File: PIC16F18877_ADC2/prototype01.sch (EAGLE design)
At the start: 18 parts, among them CN1 PIC_CN_H, CN2 12V_IN, CN3 ADC_IN, SW1 10-XX, U1 XC6202P502TB, U2 PIC16F18877-I/P, X1 20MHz

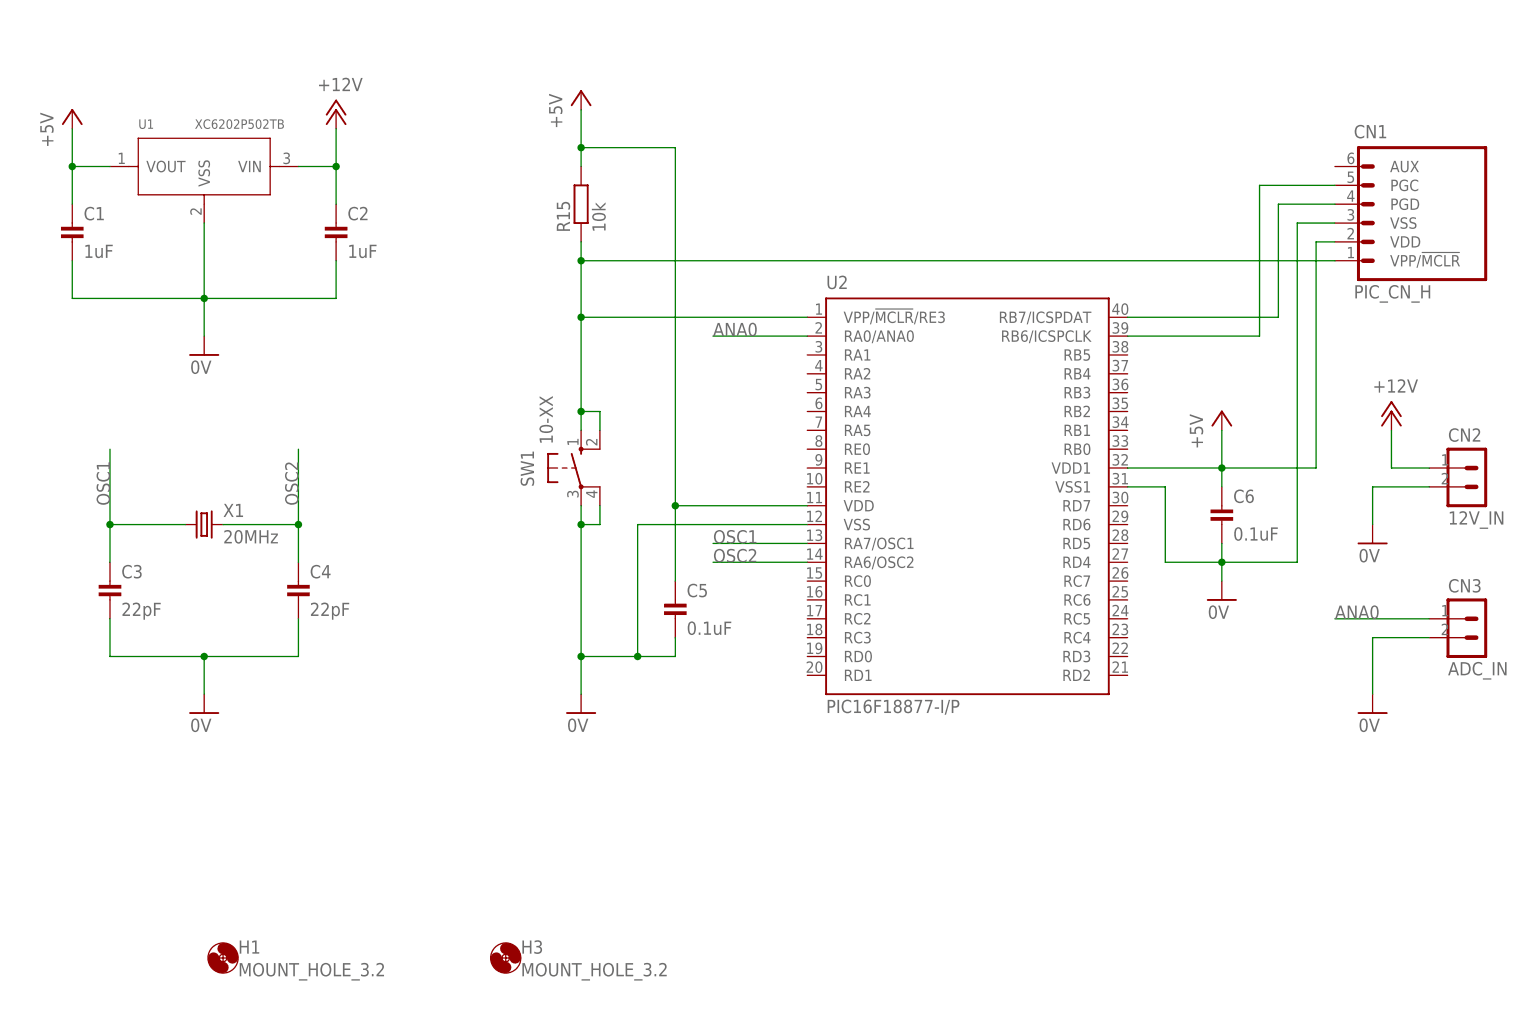
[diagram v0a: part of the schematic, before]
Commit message: 回路図を修正
LCDモジュール(AE-AQM1602A)を回路に追加
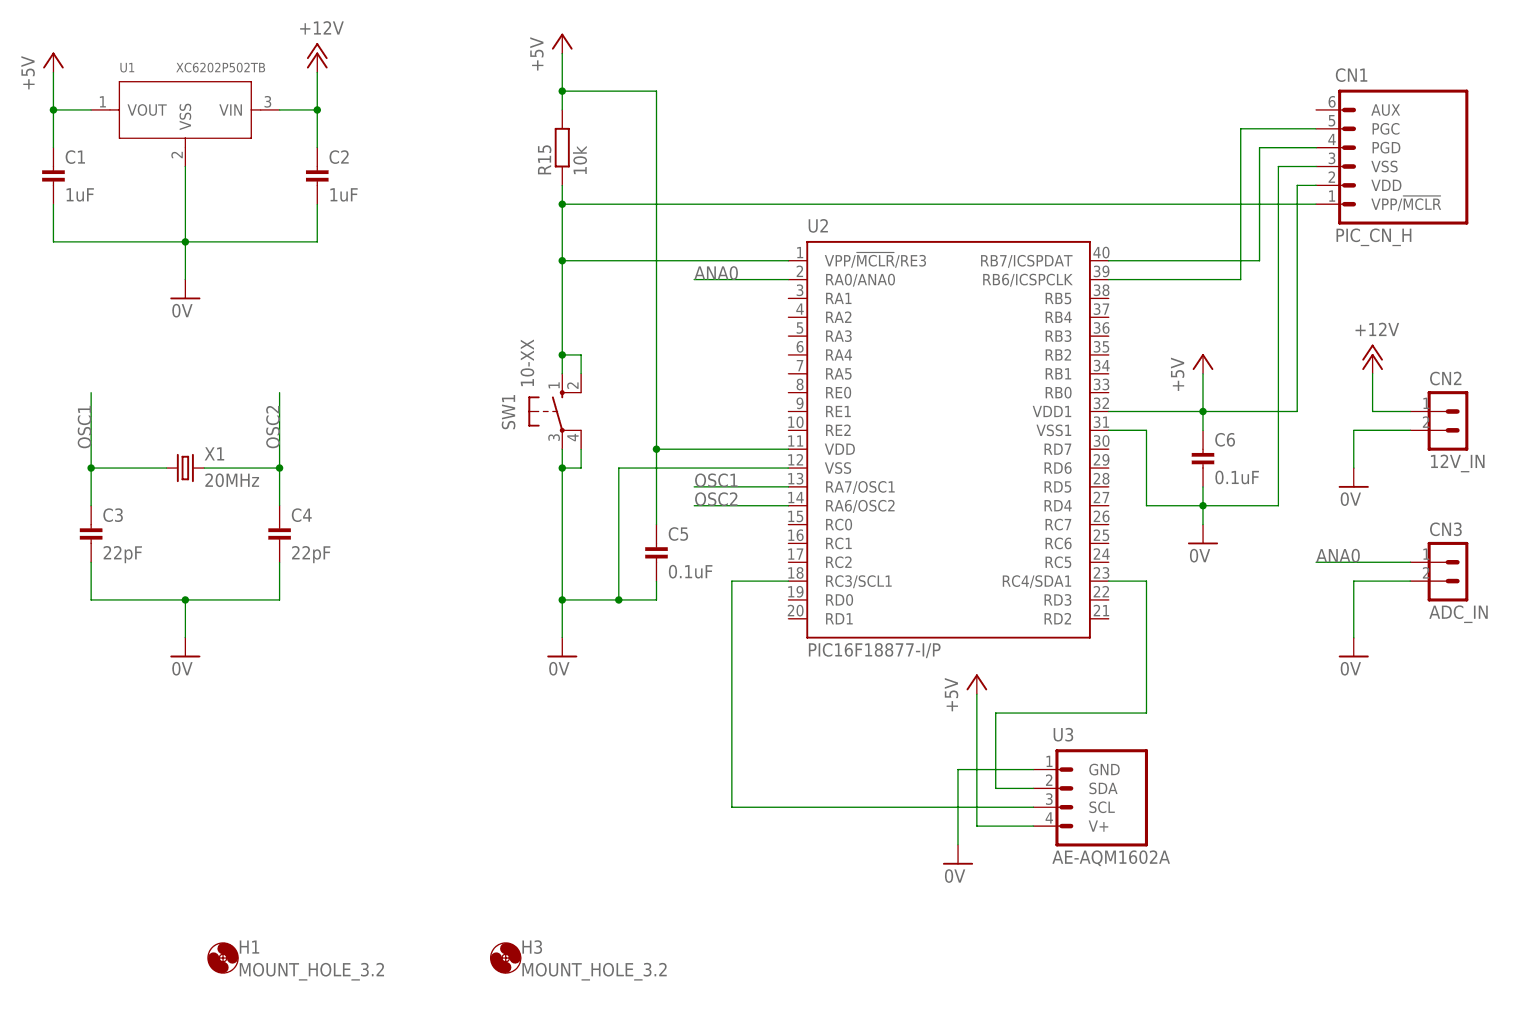
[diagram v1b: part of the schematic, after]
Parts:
- added U3: AE-AQM1602A, PartsForProto:AE-AQM1602A
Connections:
- new net N$1: U2.RC3/SCL1, U3.SCL
- new net N$5: U2.RC4/SDA1, U3.SDA
- net +5V: now also U3.V+
- net 0V: now also U3.GND
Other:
- moved on the sheet: C1, C2, C3, C4, C5, C6, CN1, CN2, CN3, R15, SW1, U1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

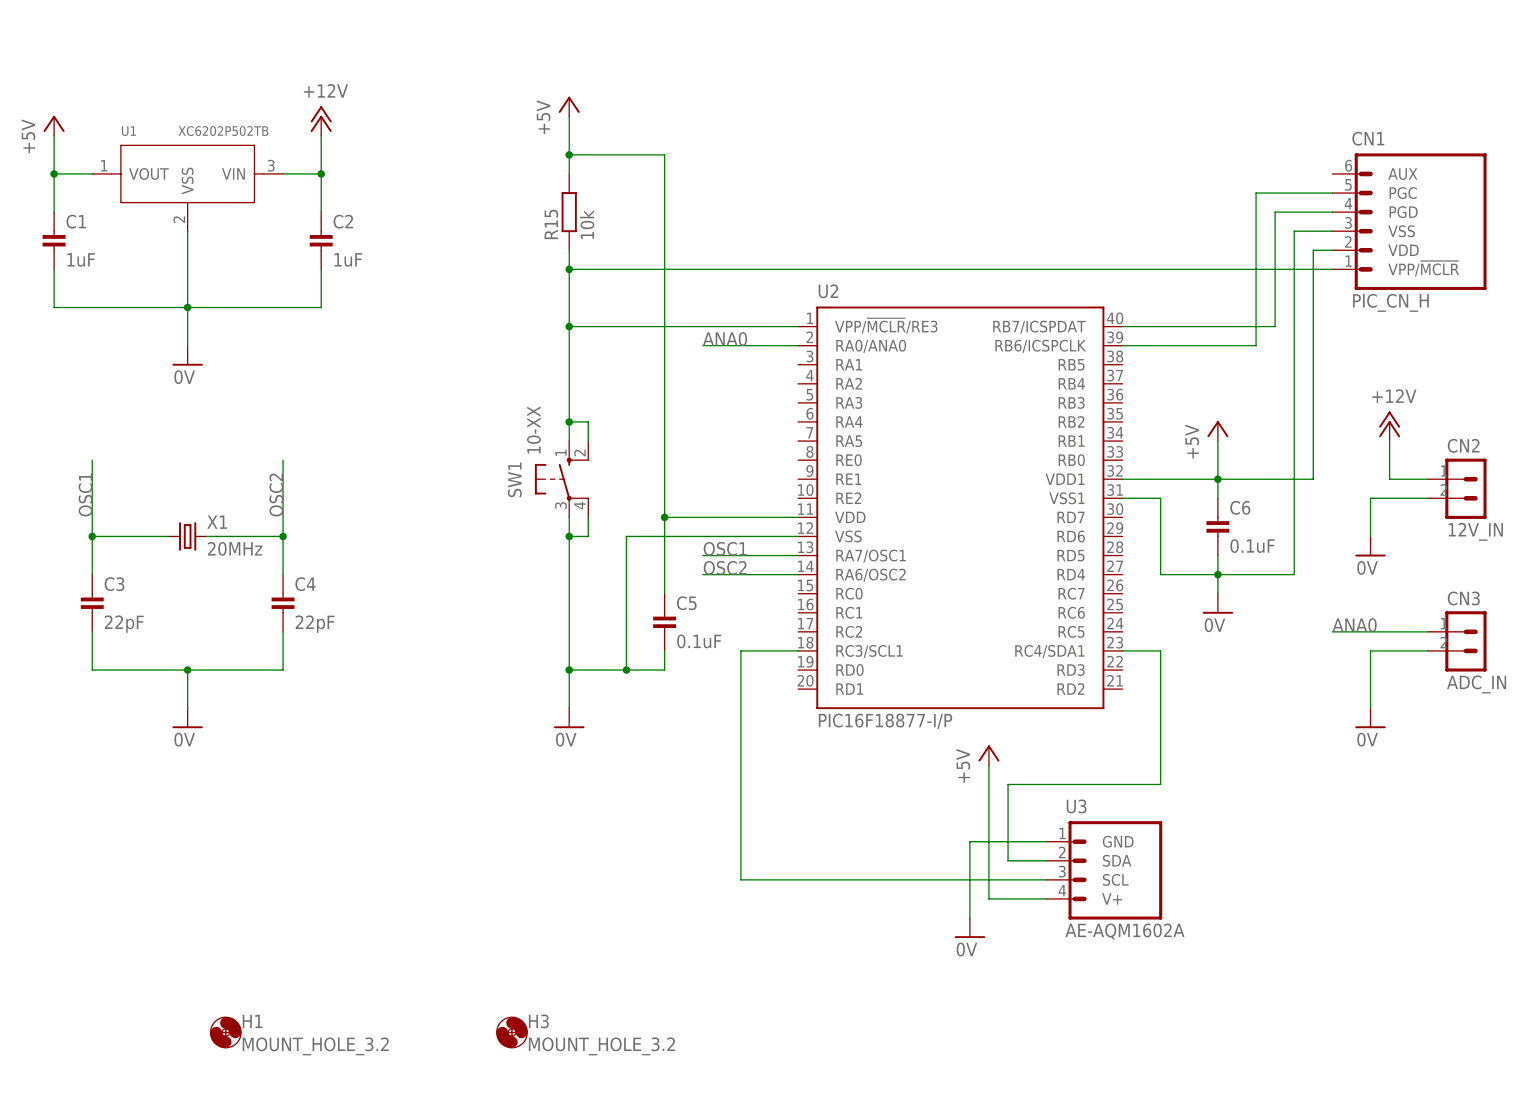
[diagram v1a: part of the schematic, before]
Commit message: I2C LCD開通時の回路図
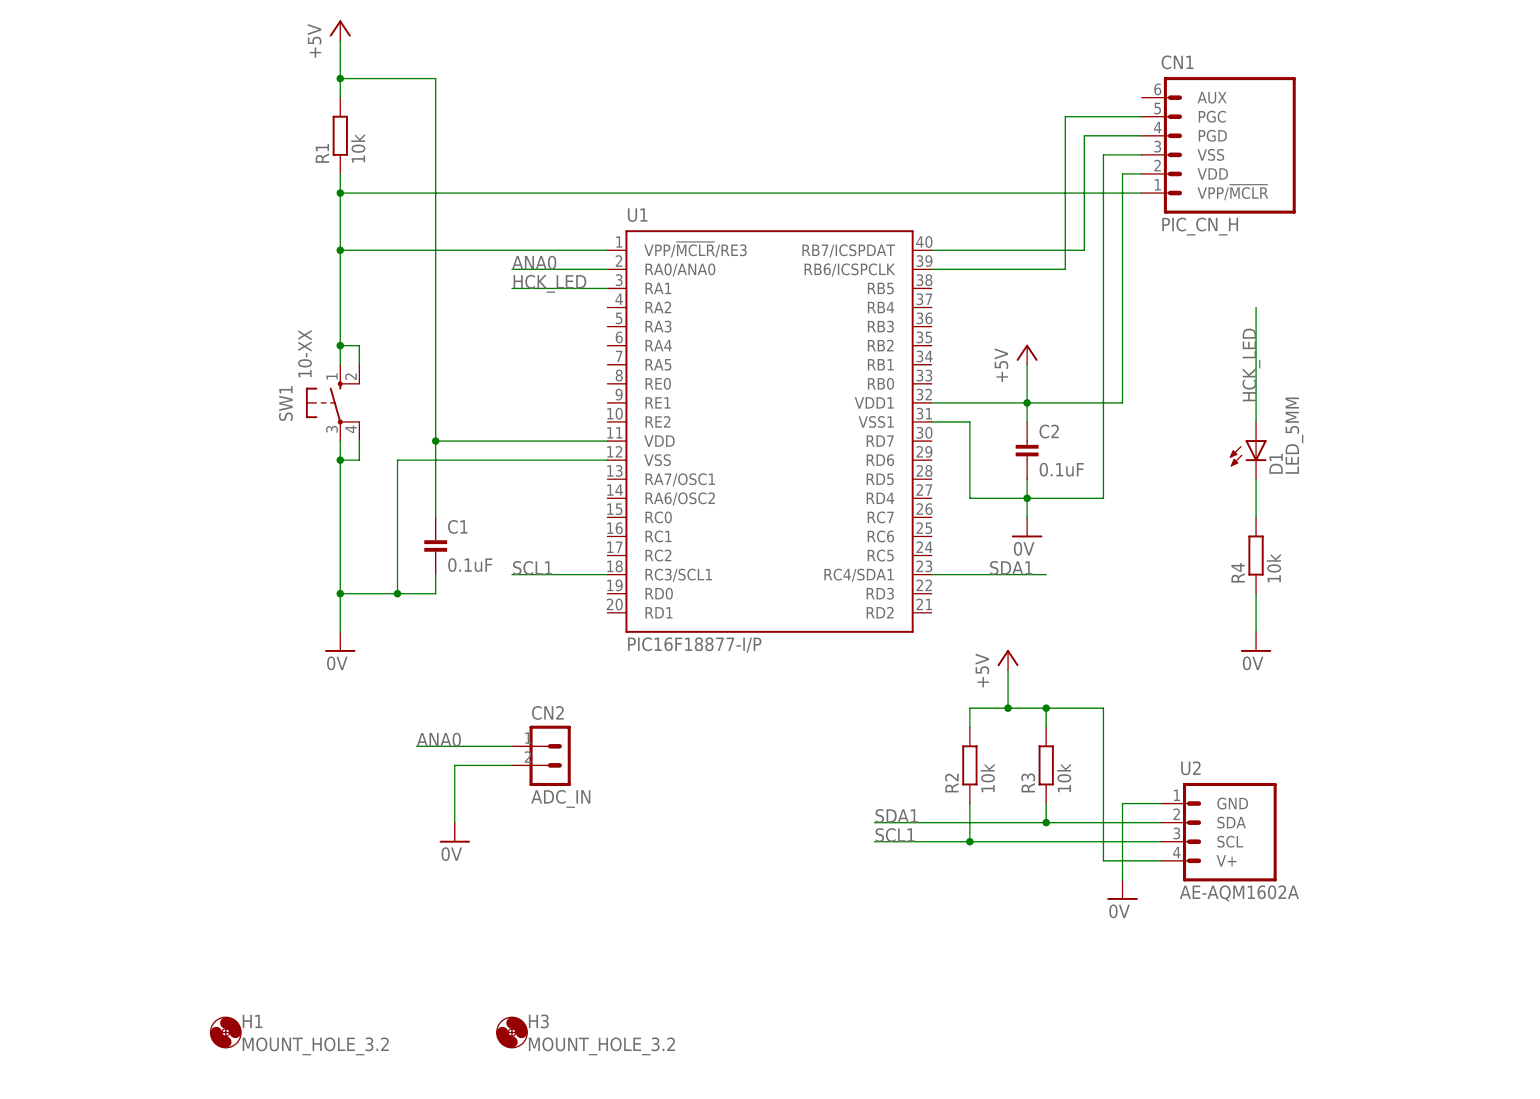
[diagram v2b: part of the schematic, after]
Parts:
- removed C3, C4: 22pF, Parts:CAP_200MIL
- removed C5, C6: 0.1uF, Parts:CAP_200MIL
- removed CN3: ADC_IN, Connectors:CONN_2PIN-L
- removed R15: 10k, Parts:RESISTOR_300MIL
- removed U3: AE-AQM1602A, PartsForProto:AE-AQM1602A
- removed X1: 20MHz, Parts:HUSG-20.000-20
- added D1: LED_5MM, Parts:LED_5MM
- added R1, R2, R3, R4: 10k, Parts:RESISTOR_300MIL
- C1, C2: value 1uF -> 0.1uF
- CN2: value 12V_IN -> ADC_IN
- U1: value XC6202P502TB -> PIC16F18877-I/P; device Parts:XC6202P502TB -> Parts:PIC16F18877-I/P
- U2: value PIC16F18877-I/P -> AE-AQM1602A; device Parts:PIC16F18877-I/P -> PartsForProto:AE-AQM1602A
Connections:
- removed net +12V: C2.1, CN2.1, U1.VIN
- removed net N$5: U2.RC4/SDA1, U3.SDA
- removed net OSC1: C3.1, U2.RA7/OSC1, X1.1
- removed net OSC2: C4.1, U2.RA6/OSC2, X1.2
- new net HCK_LED: D1.A, U1.RA1
- new net SCL1: R2.1, U1.RC3/SCL1, U2.SCL
- new net SDA1: R3.1, U1.RC4/SDA1, U2.SDA
- net +5V: now also C2.1, R1.2, R2.2, R3.2, U1.VDD, U1.VDD1, U2.V+; no longer C5.1, C6.1, R15.2, U1.VOUT, U2.VDD, U2.VDD1, U3.V+
- net 0V: now also R4.1, U1.VSS1, U2.GND; no longer C3.2, C4.2, C5.2, C6.2, CN3.2, U2.VSS, U2.VSS1, U3.GND
- net ANA0: now also CN2.1, U1.RA0/ANA0; no longer CN3.1, U2.RA0/ANA0
- net N$1: now also D1.C, R4.2; no longer U2.RC3/SCL1, U3.SCL
- net N$2: now also U1.RB7/ICSPDAT; no longer U2.RB7/ICSPDAT
- net N$3: now also R1.1, U1.VPP/!MCLR!/RE3; no longer R15.1, U2.VPP/!MCLR!/RE3
- net N$4: now also U1.RB6/ICSPCLK; no longer U2.RB6/ICSPCLK
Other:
- moved on the sheet: C1, C2, CN1, CN2, SW1

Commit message: 配線を修正
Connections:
- net HCK_LED: now also U1.RD2; no longer U1.RA1
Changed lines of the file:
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@@
 <net name="HCK_LED" class="0">
-<segment>
-<pinref part="U1" gate="G$1" pin="RA1"/>
-<wire x1="109.22" y1="129.54" x2="96.52" y2="129.54" width="0.1524" layer="91"/>
-<label x="96.52" y="129.54" size="1.778" layer="95"/>
-</segment>
 <segment>
 <wire x1="195.58" y1="111.76" x2="195.58" y2="127" width="0.1524" layer="91"/>
@@
 <pinref part="D1" gate="G$1" pin="A"/>
 </segment>
+<segment>
+<pinref part="U1" gate="G$1" pin="RD2"/>
+<wire x1="152.4" y1="86.36" x2="167.64" y2="86.36" width="0.1524" layer="91"/>
+<label x="154.94" y="86.36" size="1.778" layer="95"/>
+</segment>
 </net>
